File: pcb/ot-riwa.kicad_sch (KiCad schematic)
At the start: 0 parts

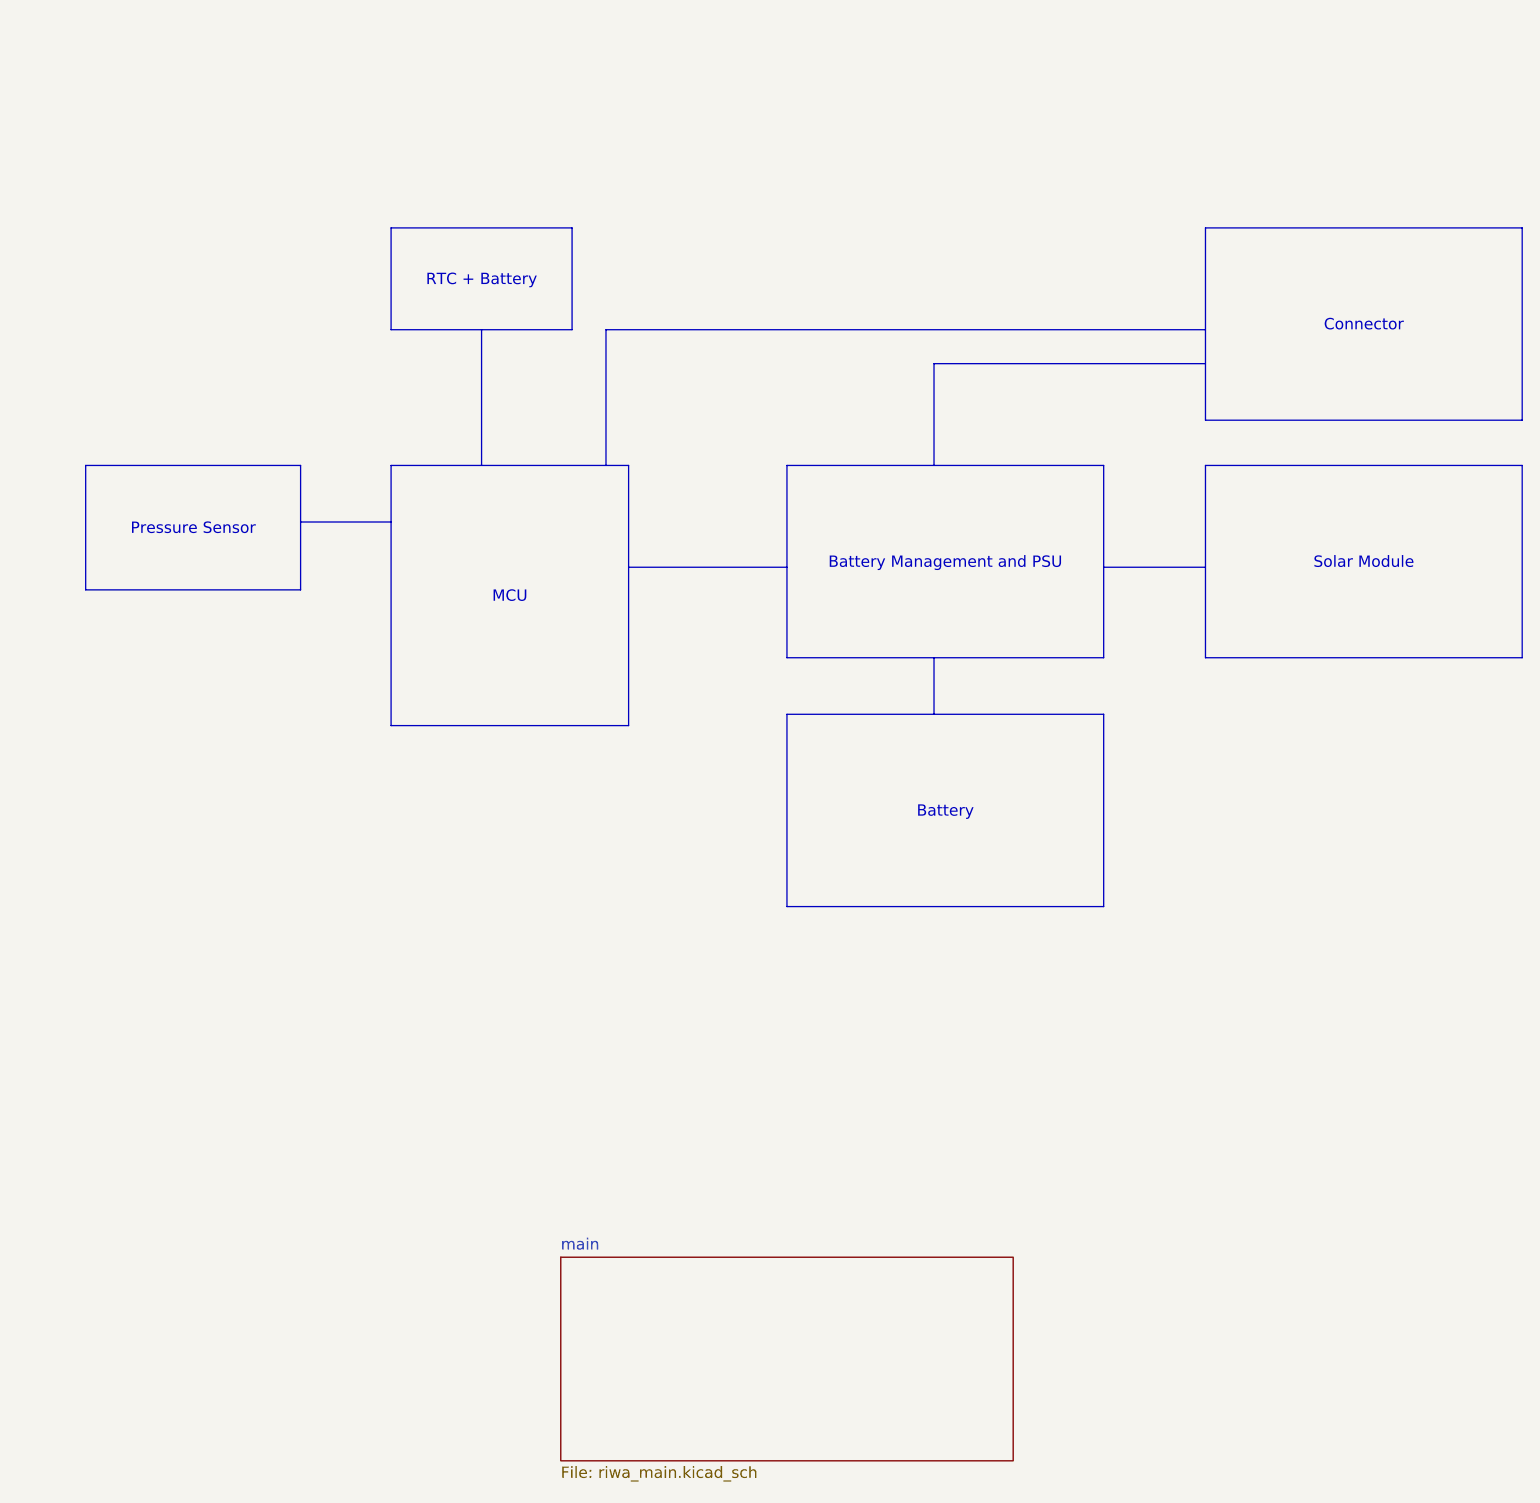
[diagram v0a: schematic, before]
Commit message: Placed components on PCB Board (no layouting)
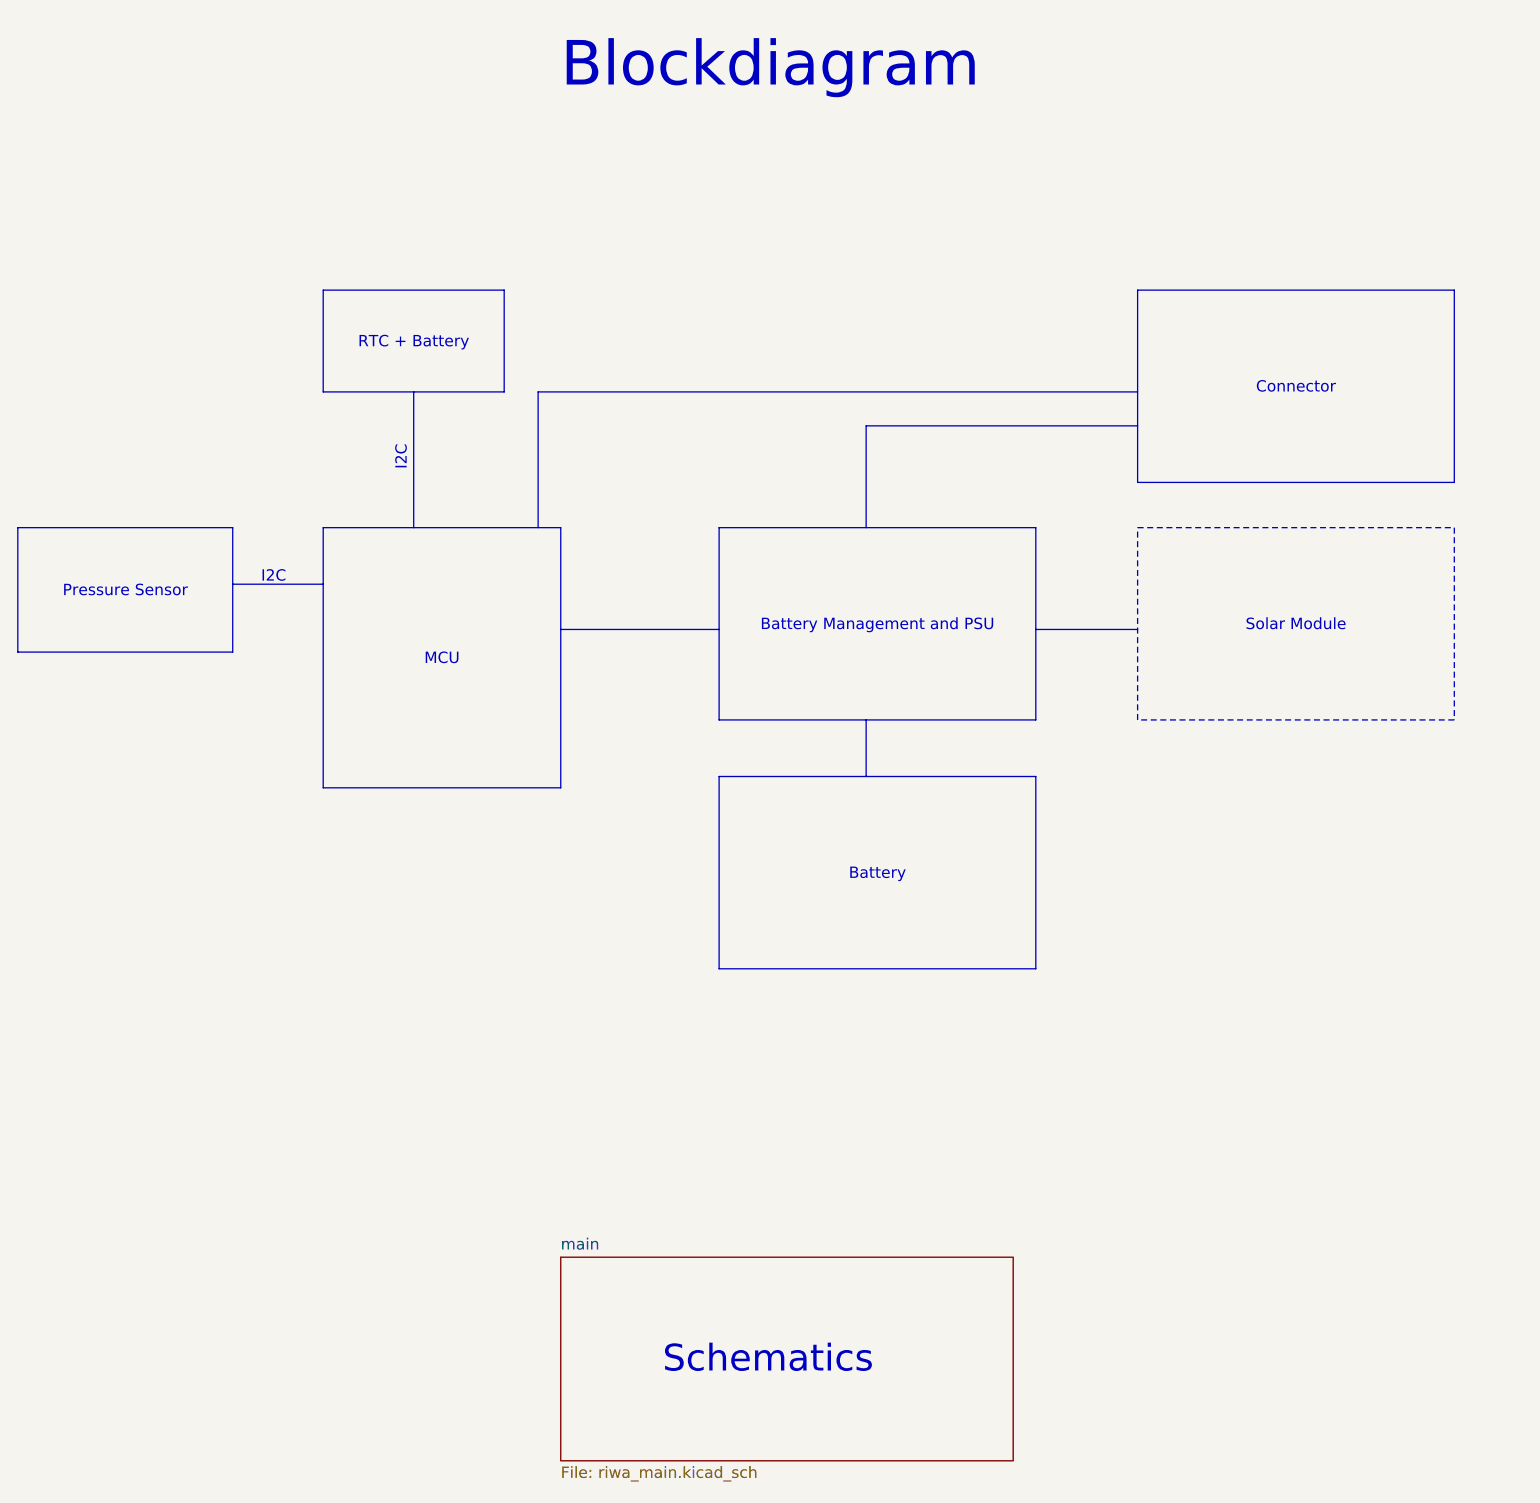
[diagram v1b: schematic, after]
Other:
- note added: "Blockdiagram"
- note added: "I2C"
- note added: "Schematics"
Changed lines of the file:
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@@
 (kicad_sch (version 20230121) (generator eeschema)
   (paper "A4")
-  (polyline (pts (xy 87.63 83.82) (xy 97.79 83.82))
+  (polyline (pts (xy 80.01 90.805) (xy 90.17 90.805))
     (stroke (width 0) (type default))
   )
-  (polyline (pts (xy 121.92 62.23) (xy 121.92 77.47))
+  (polyline (pts (xy 114.3 69.215) (xy 114.3 84.455))
     (stroke (width 0) (type default))
   )
-  (polyline (pts (xy 158.75 66.04) (xy 158.75 77.47))
+  (polyline (pts (xy 151.13 73.025) (xy 151.13 84.455))
     (stroke (width 0) (type default))
   )
-  (polyline (pts (xy 189.23 66.04) (xy 158.75 66.04))
+  (polyline (pts (xy 181.61 73.025) (xy 151.13 73.025))
     (stroke (width 0) (type default))
   )
-  (polyline (pts (xy 107.95 62.23) (xy 107.95 77.47))
+  (polyline (pts (xy 100.33 69.215) (xy 100.33 84.455))
     (stroke (width 0) (type default))
   )
-  (polyline (pts (xy 158.75 99.06) (xy 158.75 105.41))
+  (polyline (pts (xy 151.13 106.045) (xy 151.13 112.395))
     (stroke (width 0) (type default))
   )
-  (polyline (pts (xy 189.23 62.23) (xy 121.92 62.23))
+  (polyline (pts (xy 181.61 69.215) (xy 114.3 69.215))
     (stroke (width 0) (type default))
   )
-  (polyline (pts (xy 124.46 88.9) (xy 142.24 88.9))
+  (polyline (pts (xy 116.84 95.885) (xy 134.62 95.885))
     (stroke (width 0) (type default))
   )
-  (polyline (pts (xy 177.8 88.9) (xy 189.23 88.9))
+  (polyline (pts (xy 170.18 95.885) (xy 181.61 95.885))
     (stroke (width 0) (type default))
   )
   (text_box "Connector"
-    (at 189.23 50.8 0) (size 35.56 21.59)
+    (at 181.61 57.785 0) (size 35.56 21.59)
     (stroke (width 0) (type default))
     (fill (type none))
@@
   )
   (text_box "Pressure Sensor"
-    (at 63.5 77.47 0) (size 24.13 13.97)
+    (at 55.88 84.455 0) (size 24.13 13.97)
     (stroke (width 0) (type default))
     (fill (type none))
@@
   )
   (text_box "RTC + Battery"
-    (at 97.79 50.8 0) (size 20.32 11.43)
+    (at 90.17 57.785 0) (size 20.32 11.43)
     (stroke (width 0) (type default))
     (fill (type none))
@@
   )
   (text_box "Battery Management and PSU\n"
-    (at 142.24 77.47 0) (size 35.56 21.59)
+    (at 134.62 84.455 0) (size 35.56 21.59)
     (stroke (width 0) (type default))
     (fill (type none))
@@
   )
   (text_box "MCU"
-    (at 97.79 77.47 0) (size 26.67 29.21)
+    (at 90.17 84.455 0) (size 26.67 29.21)
     (stroke (width 0) (type default))
     (fill (type none))
@@
   )
   (text_box "Solar Module"
-    (at 189.23 77.47 0) (size 35.56 21.59)
+    (at 181.61 84.455 0) (size 35.56 21.59)
+    (stroke (width 0) (type dot))
+    (fill (type none))
+    (effects (font (size 1.27 1.27)))
+  )
+  (text_box "Battery"
+    (at 134.62 112.395 0) (size 35.56 21.59)
     (stroke (width 0) (type default))
     (fill (type none))
     (effects (font (size 1.27 1.27)))
   )
-  (text_box "Battery"
-    (at 142.24 105.41 0) (size 35.56 21.59)
-    (stroke (width 0) (type default))
-    (fill (type none))
-    (effects (font (size 1.27 1.27)))
+  (text "I2C" (at 99.695 78.105 90)
+    (effects (font (size 1.27 1.27)) (justify left bottom))
+  )
+  (text "I2C" (at 83.185 90.805 0)
+    (effects (font (size 1.27 1.27)) (justify left bottom))
+  )
+  (text "Blockdiagram" (at 116.84 35.56 0)
+    (effects (font (size 5 5)) (justify left bottom))
+  )
+  (text "Schematics" (at 128.27 179.705 0)
+    (effects (font (size 3 3)) (justify left bottom))
   )
   (sheet (at 116.84 166.37) (size 50.8 22.86) (fields_autoplaced)
